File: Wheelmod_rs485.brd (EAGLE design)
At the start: 42 x 40 mm, 53 parts, among them U1 ATMEGA8U2AU, U2 SI8441IS1, U3 MC33887-HSOP, U4 NFET-SOIC8, U5 LDO, X1 MINI-USB, X3 ENC, X5 LOGIC_IN, X6 R485-IO, Y1 SMDRESONATOR

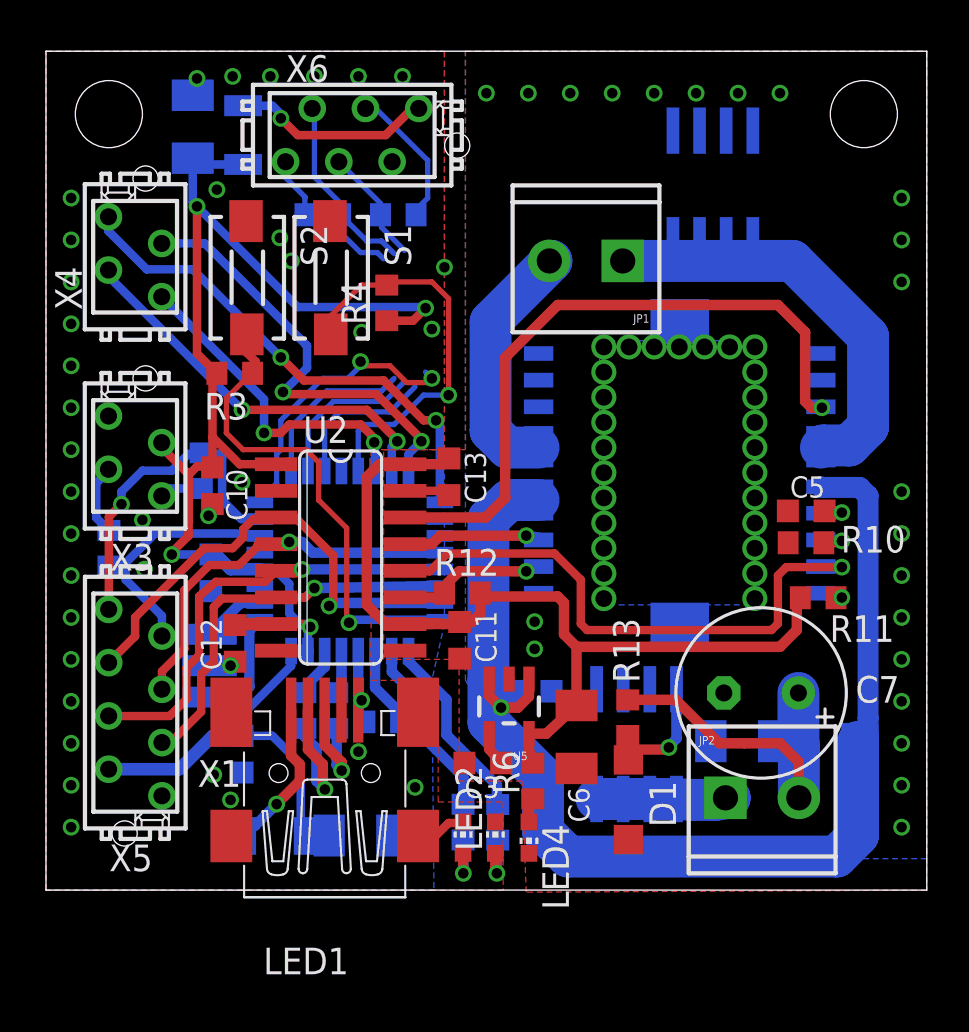
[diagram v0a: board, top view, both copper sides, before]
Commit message: Rerouted USB dongle
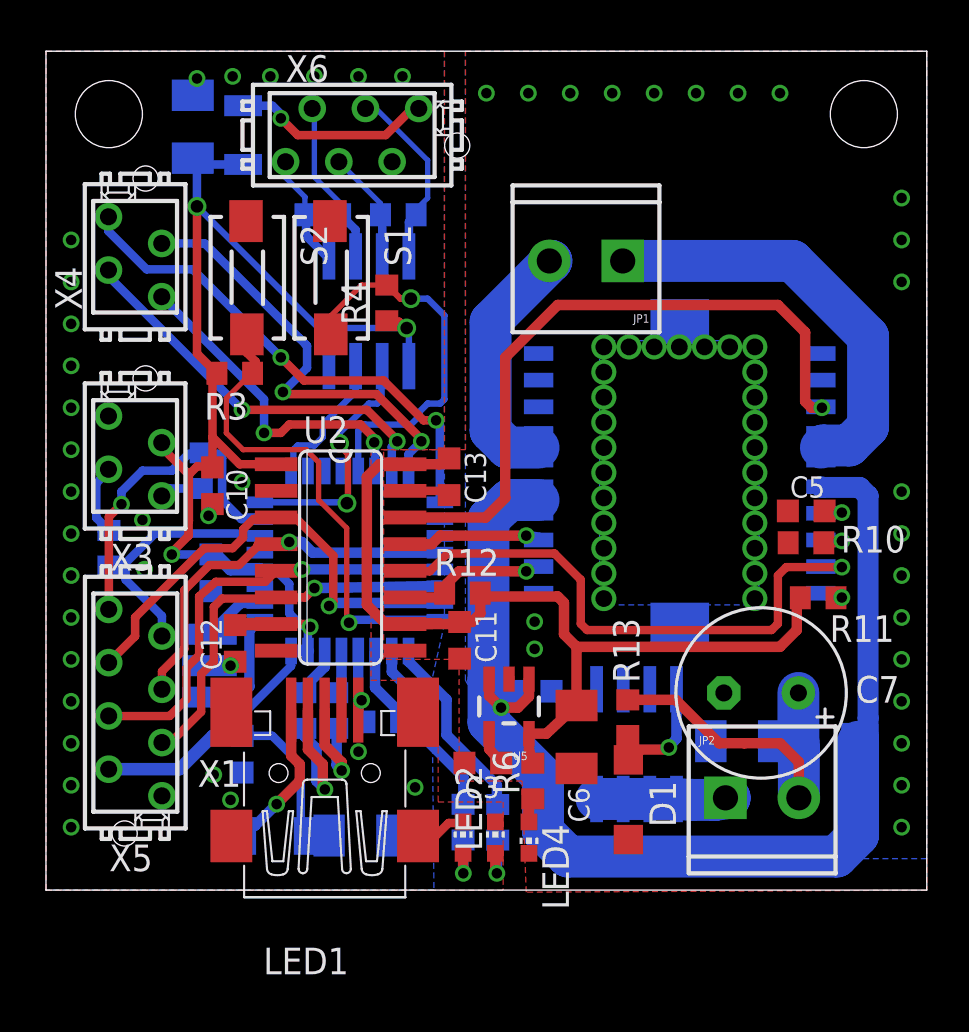
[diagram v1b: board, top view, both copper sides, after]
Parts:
- moved U$2 17.5 mm to (15.4, 27.6)
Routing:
- net DE: track 7.61 -> 0.00 mm
- net RE: track 7.21 -> 0.00 mm
- net A: track 6.89 -> 9.01 mm
- net Y: track 7.55 -> 5.46 mm
- net RX: track 13.7 -> 12.0 mm
- net TX: track 7.99 -> 6.74 mm
- net Z: track 8.95 -> 7.91 mm
- net N$2: track 19.0 -> 18.5 mm
- net GND: vias 38 -> 31
